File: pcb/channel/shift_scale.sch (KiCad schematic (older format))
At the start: 5 parts

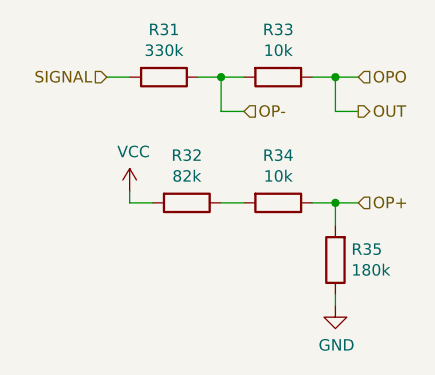
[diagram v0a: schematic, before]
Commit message: Substitute available resistor values
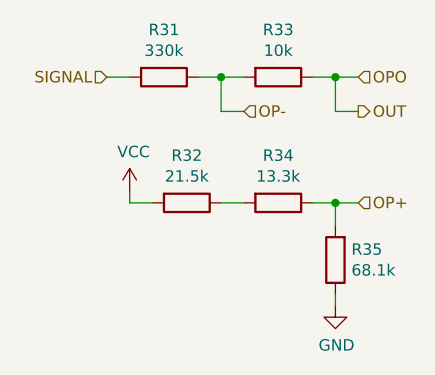
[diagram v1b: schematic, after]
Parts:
- R32: value 82k -> 21.5k
- R34: value 10k -> 13.3k
- R35: value 180k -> 68.1k
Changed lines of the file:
@@
 P 5400 4350
 F 0 "R32" V 5193 4350 50  0000 C CNN
-F 1 "82k" V 5284 4350 50  0000 C CNN
+F 1 "21.5k" V 5284 4350 50  0000 C CNN
 F 2 "Resistor_SMD:R_0603_1608Metric_Pad1.05x0.95mm_HandSolder" V 5330 4350 50  0001 C CNN
 F 3 "~" H 5400 4350 50  0001 C CNN
@@
 P 5800 4350
 F 0 "R34" V 5593 4350 50  0000 C CNN
-F 1 "10k" V 5684 4350 50  0000 C CNN
+F 1 "13.3k" V 5684 4350 50  0000 C CNN
 F 2 "Resistor_SMD:R_0603_1608Metric_Pad1.05x0.95mm_HandSolder" V 5730 4350 50  0001 C CNN
 F 3 "~" H 5800 4350 50  0001 C CNN
@@
 P 6050 4600
 F 0 "R35" H 5980 4554 50  0000 R CNN
-F 1 "180k" H 5980 4645 50  0000 R CNN
+F 1 "68.1k" H 5980 4645 50  0000 R CNN
 F 2 "Resistor_SMD:R_0603_1608Metric_Pad1.05x0.95mm_HandSolder" V 5980 4600 50  0001 C CNN
 F 3 "~" H 6050 4600 50  0001 C CNN
